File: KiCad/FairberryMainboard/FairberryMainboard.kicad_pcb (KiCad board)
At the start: 2 copper layers, 39.7 x 19.3 mm, 19 parts, among them J1 USB_Header, J2 Conn_02x03_Odd_Even, J3 Conn_02x02_Odd_Even, J4 Conn_01x02, U1 ATmega32U4-MU, U2 BBQ10KBD, Y1 Crystal_GND24

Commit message: Kicad files for mainboard v0.2.0
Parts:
- moved R2 0.85 mm to (179.1, 95.5)
- moved R3 0.85 mm to (179.1, 93.9)
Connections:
- J3 pad 3: Net-(C3-Pad1) -> Net-(U1-Pad39)
- J3 pad 4: Net-(J3-Pad4) -> Net-(U1-Pad38)
- U1 pad 1: unconnected-(U1-Pad1) -> Net-(U1-Pad1)
- U1 pad 39: Net-(J3-Pad4) -> Net-(U1-Pad39)
- U2 pad 8: Net-(U1-Pad38) -> Net-(U1-Pad1)
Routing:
- net Net-(J3-Pad4): track 15.7 -> 0.00 mm, vias 2 -> 0
- net Net-(U1-Pad1): track 0.00 -> 13.7 mm, vias 0 -> 2
- net Net-(U1-Pad39): track 0.00 -> 13.0 mm, vias 0 -> 2
- net Net-(C3-Pad1): track 10.7 -> 1.62 mm, vias 2 -> 0
- net Net-(U1-Pad38): track 11.0 -> 16.7 mm, vias 0 -> 2
- net Net-(J2-Pad5): track 44.1 -> 40.3 mm
- net /USB_UC_D-: track 13.1 -> 14.3 mm
- net Net-(U1-Pad21): track 23.2 -> 22.0 mm
- net /USB_Plug_D+: track 17.6 -> 16.6 mm
- net Net-(U1-Pad22): track 20.3 -> 19.4 mm
- net /USB_Plug_D-: track 21.3 -> 20.4 mm
- net Net-(J3-Pad1): track 14.6 -> 13.8 mm
- net VCC: track 77.1 -> 77.9 mm
- net Net-(J2-Pad1): track 42.4 -> 43.1 mm
- net Net-(J2-Pad3): track 40.7 -> 41.2 mm
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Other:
- board text added: "+"
- board text added: "-"
- board text added: "10.07.2022 Fairberry v0.2.0 ©Dakkaron, 2022"
- board text added: "A2"
- board text added: "A3"
- board text added: "A4"
- board text added: "A5"
- board text added: "D+"
- board text added: "D-"
- board text added: "D2"
- board text added: "D3"
- board text removed: "30.6.2022 Fairberry v0.1.1 ©Dakkaron, 2022"

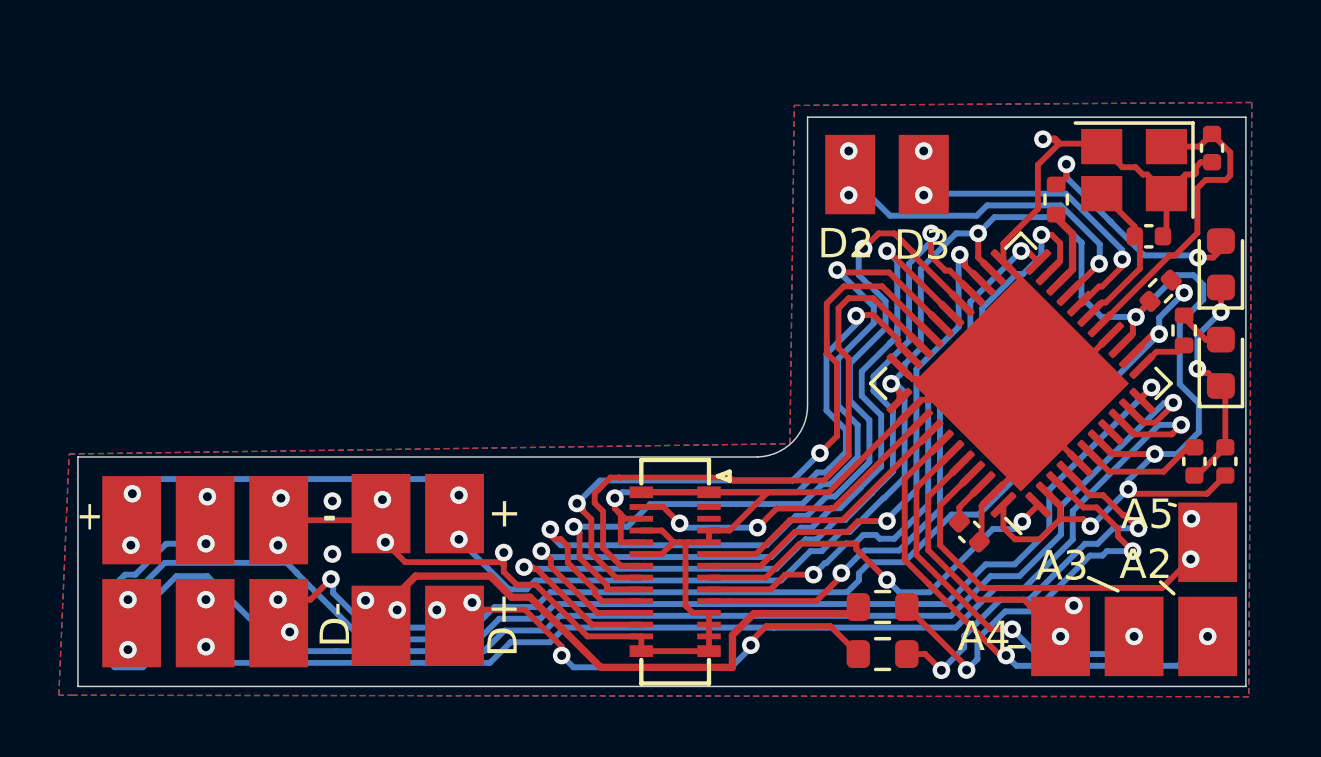
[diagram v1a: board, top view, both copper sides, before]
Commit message: Hardware revision v0.3.0 (#16) (#19)
* Split backlight into two zones, removed status LEDs, reduced y size by 1mm

* Made firmware compatible with v0.3.0 (doesn't make use of dual backlight controls yet), refactoring

* Improved Case Generator script, added presets for Fairphone 4 and Samsung Galaxy A54

* Finalisation of v0.3.0 PCB

* License/Version header for firmware

* Removed generated stl
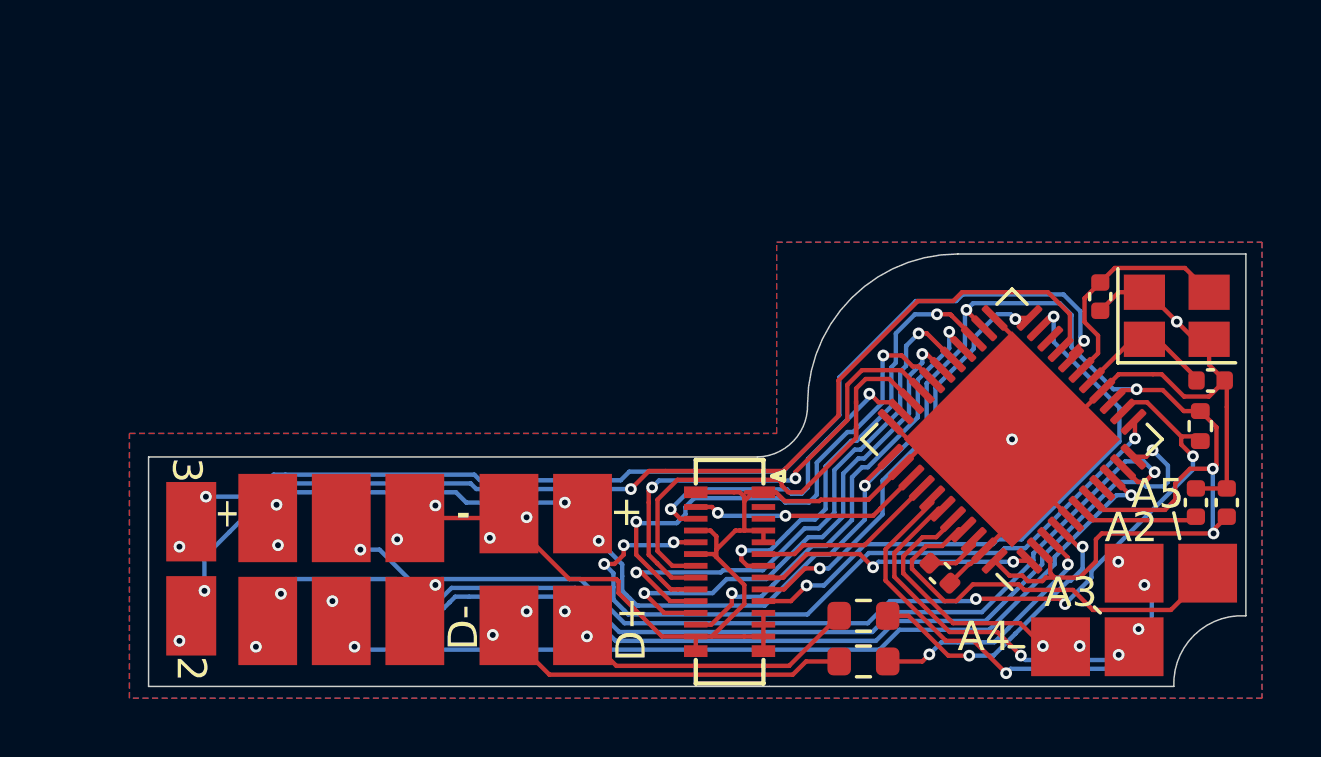
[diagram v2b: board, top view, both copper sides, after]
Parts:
- removed D1: LED Blue, LED_SMD:LED_0603_1608Metric
- removed D2: LED Yellow, LED_SMD:LED_0603_1608Metric
- removed R4: 470, Resistor_SMD:R_0402_1005Metric
- removed R5: 680, Resistor_SMD:R_0402_1005Metric
- ?: renamed from J4; footprint Fairberry:TestPoint_Pad_1x2_2.0x3.0mm -> Fairberry:TestPoint_Pad_1x2_2.0x3.0mm_Rotated
- ?: renamed from J3; footprint Fairberry:TestPoint_Pad_1+3_2.0x3.0mm_slim -> Fairberry:TestPoint_Pad_2+2_Z_2.0x2.0mm
- moved ? 27.0 mm to (155.6, 94.2), turned to 90 degrees
- moved C4 7.90 mm to (190.2, 86.2), turned to 0 degrees
- moved Y1 5.16 mm to (189.1, 84.0), turned to 0 degrees
- moved R1 4.79 mm to (189.9, 87.8), turned to -90 degrees
- moved J2 4.63 mm to (158.2, 90.9)
- moved J1 4.35 mm to (166.4, 90.9)
- moved C5 2.63 mm to (186.5, 83.3), turned to -90 degrees
- moved R3 1.96 mm to (178.4, 95.8)
- moved U1 1.92 mm to (183.5, 88.2)
- moved U2 1.85 mm to (173.9, 92.7)
- moved C3 1.72 mm to (181.1, 92.8)
- moved R2 1.45 mm to (178.4, 94.2)
- moved C1 1.40 mm to (189.8, 90.3), turned to 90 degrees
- moved C2 1.40 mm to (190.8, 90.3)
- moved ? 0.70 mm to (187.7, 92.5)
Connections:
- U1 pad 12: Net-(R4-Pad1) -> Net-(U1-Pad12)
- U1 pad 20: Net-(R5-Pad1) -> unconnected-(U1-Pad20)
- U2 pad 24: Net-(U1-Pad32) -> Net-(U1-Pad12)
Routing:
- net Net-(J4-Pad2): track 11.6 -> 37.7 mm
- net Net-(U1-Pad12): track 0.00 -> 25.9 mm, vias 0 -> 4
- net Net-(J4-Pad1): track 13.1 -> 38.8 mm
- net Net-(J2-Pad4): track 53.7 -> 32.6 mm, vias 3 -> 2
- net Net-(U1-Pad26): track 30.6 -> 15.8 mm
- net Net-(U1-Pad28): track 29.3 -> 17.5 mm
- net Net-(U1-Pad27): track 30.1 -> 18.9 mm
- net VCC: track 77.9 -> 67.3 mm, vias 10 -> 9
- net GND: track 88.7 -> 78.6 mm, vias 10 -> 6
- net Net-(J2-Pad3): track 41.2 -> 31.5 mm
- net Net-(U1-Pad32): track 19.8 -> 11.6 mm
- net Net-(U1-Pad29): track 26.3 -> 18.3 mm
- net Net-(D2-Pad2): track 7.87 -> 0.00 mm, vias 2 -> 0
- net Net-(J2-Pad5): track 40.3 -> 33.5 mm, vias 5 -> 4
- net /USB_Plug_D-: track 20.4 -> 13.8 mm
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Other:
- board size 39.7 x 19.3 mm -> 37.3 x 14.7 mm
- board text added: "07.03.2024 Fairberry v0.3.0 ©Dakkaron, 2024"
- board text added: "2"
- board text added: "3"
- board text removed: "10.07.2022 Fairberry v0.2.0 ©Dakkaron, 2022"
- board text removed: "D2"
- board text removed: "D3"
